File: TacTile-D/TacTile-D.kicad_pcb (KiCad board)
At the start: 2 copper layers, 60 x 60 mm, 17 parts, among them J1 Conn_01x06, J2 Conn_01x06, J3 Conn_01x06, J4 Conn_01x06, J5 Conn_01x04, J6 Conn_01x05, J7 Conn_01x02, J8 Conn_01x02, U1 74LS04, U2 4011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

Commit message: Updated more fabrication files and D board selecting wrong coil
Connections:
- U1 pad 5: Net-(U3-QD) -> (no net)
- U1 pad 6: LEN -> (no net)
- U2 pad 11: (no net) -> LEN
- U2 pad 12: (no net) -> Net-(U3-RCLK)
- U2 pad 13: (no net) -> Net-(U3-QD)
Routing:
- net Net-(U3-RCLK): track 48.8 -> 87.0 mm, vias 1 -> 2
- net Net-(U3-QD): track 44.6 -> 46.8 mm, vias 1 -> 0
- net LEN: track 40.4 -> 41.8 mm
- net Net-(U5A-D): track 45.6 -> 46.6 mm
- net MOSI: track 95.5 -> 96.0 mm

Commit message: Fixed issues with D board and rerouted
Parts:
- removed U8: 4042, Package_DIP:DIP-16_W7.62mm
- moved U5 8.31 mm to (44.4, 51.8)
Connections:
- U1 pad 2: Net-(U4-CPR) -> ACLK
- U1 pad 5: (no net) -> Net-(U1-Pad5)
- U1 pad 6: (no net) -> Net-(U5B-D)
- U2 pad 4: Net-(U5B-~{S}) -> Net-(U1-Pad5)
- U3 pad 15: LS0 -> LS2
- U3 pad 2: LS2 -> LS0
- U4 pad 13: Net-(U4-CPR) -> ACLK
- U5 pad 10: Net-(U5B-~{S}) -> VCC
- U5 pad 11: GND -> ACLK
- U5 pad 12: GND -> Net-(U5B-D)
- U6 pad 11: (no net) -> Net-(U9-A)
- U6 pad 12: (no net) -> Net-(U5A-Q)
- U6 pad 13: (no net) -> MOSI
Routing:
- net Net-(U1-Pad5): track 0.00 -> 52.7 mm
- net ACLK: track 0.00 -> 52.6 mm
- net Net-(U5B-D): track 0.00 -> 38.3 mm, vias 0 -> 1
- net Net-(U5A-Q): track 7.19 -> 32.8 mm
- net Net-(U5B-~{S}): track 25.0 -> 0.00 mm
- net Net-(U9-A): track 31.0 -> 51.4 mm
- net Net-(U5A-D): track 46.6 -> 30.3 mm, vias 2 -> 0
- net Net-(U4-CPR): track 14.9 -> 0.00 mm
- net Net-(U5A-C): track 75.1 -> 61.0 mm
- net Net-(U3-RCLK): track 87.0 -> 73.1 mm
- net MOSI: track 96.0 -> 82.2 mm, vias 0 -> 1
- net LS2: track 11.8 -> 19.3 mm
- net Net-(U4-Q0): track 46.1 -> 52.6 mm
- net SEN: track 74.8 -> 68.8 mm, vias 0 -> 1
- net Net-(U2-Pad5): track 34.8 -> 29.0 mm
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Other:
- board text added: "D-2"
- board text added: "TacTile"
- board text added: "©CGR"

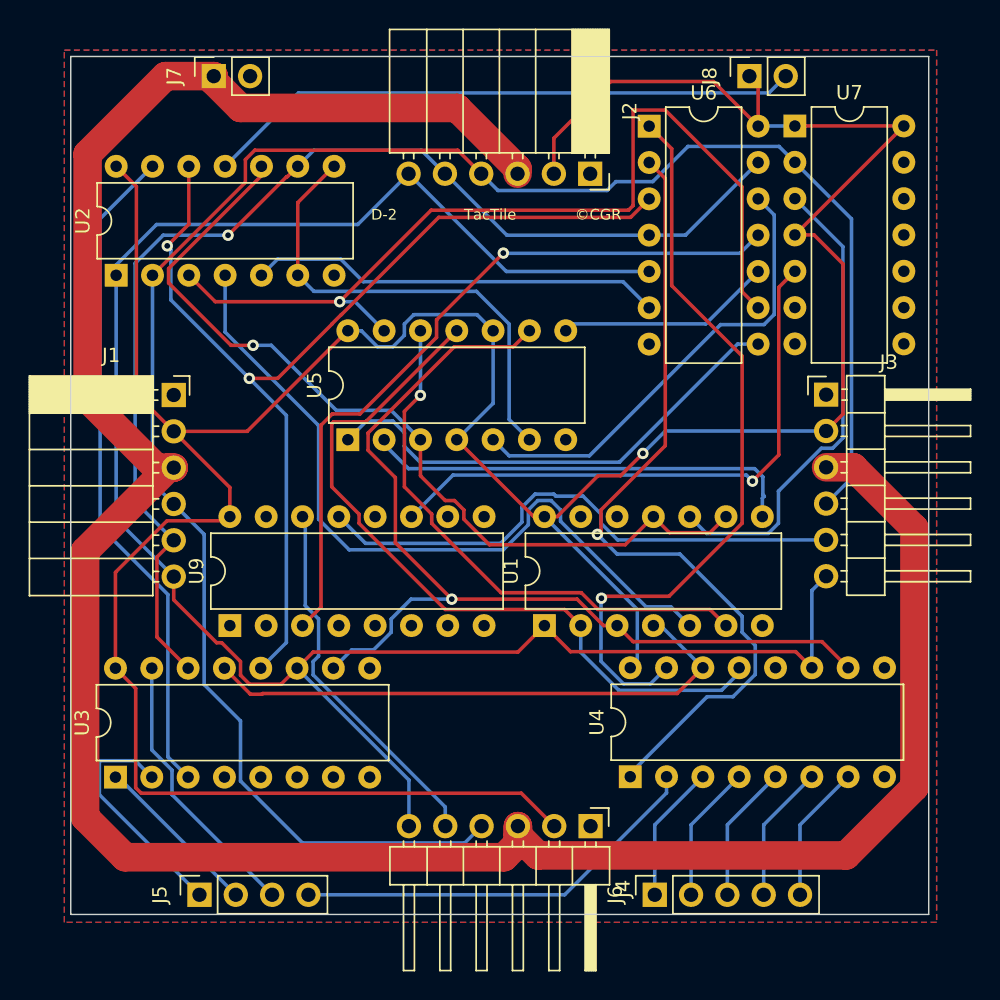
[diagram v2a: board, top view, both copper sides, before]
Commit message: Fixed counter clocking delay on D board
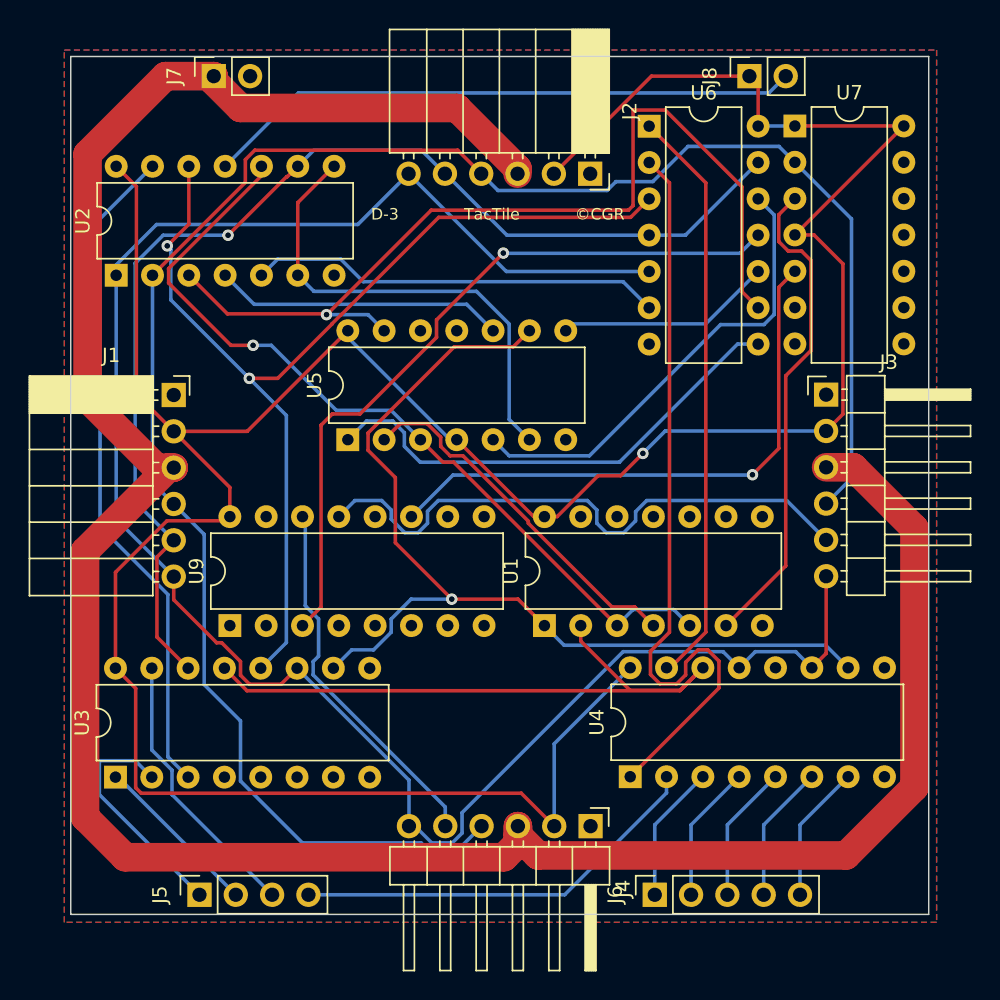
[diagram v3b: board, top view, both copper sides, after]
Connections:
- U1 pad 1: CLK -> SEN
- U1 pad 10: Net-(U7A-C) -> (no net)
- U1 pad 11: Net-(U5A-C) -> (no net)
- U1 pad 2: ACLK -> Net-(U3-~{OE})
- U1 pad 3: SEN -> Net-(U5A-C)
- U1 pad 4: Net-(U3-~{OE}) -> Net-(U5A-D)
- U1 pad 5: Net-(U1-Pad5) -> Net-(U5A-C)
- U1 pad 6: Net-(U5B-D) -> Net-(U7A-C)
- U1 pad 8: Net-(U5A-D) -> (no net)
- U1 pad 9: Net-(U5A-C) -> (no net)
- U2 pad 4: Net-(U1-Pad5) -> Net-(U5B-~{S})
- U4 pad 13: ACLK -> CLK
- U5 pad 10: VCC -> Net-(U5B-~{S})
- U5 pad 11: ACLK -> GND
- U5 pad 12: Net-(U5B-D) -> GND
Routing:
- net Net-(U1-Pad5): track 52.7 -> 0.00 mm
- net ACLK: track 52.6 -> 0.00 mm
- net Net-(U5B-D): track 38.3 -> 0.00 mm, vias 1 -> 0
- net Net-(U5B-~{S}): track 0.00 -> 20.3 mm
- net VCC: track 224.5 -> 211.0 mm
- net Net-(U4-Q0): track 52.6 -> 40.8 mm, vias 1 -> 0
- net Net-(U3-~{OE}): track 39.7 -> 46.5 mm
- net Net-(U5A-D): track 30.3 -> 25.6 mm
- net Net-(U5A-C): track 61.0 -> 58.2 mm
- net Net-(U4-Q1): track 57.2 -> 54.5 mm, vias 1 -> 0
- net MISO0: track 38.6 -> 41.2 mm
- net CLK: track 139.5 -> 137.5 mm
- net Net-(U5B-~{R}): track 64.0 -> 65.3 mm
- net Net-(U7A-C): track 33.4 -> 34.3 mm
- net Net-(U7A-Q): track 41.1 -> 40.5 mm
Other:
- board text added: "D-3"
- board text removed: "D-2"
